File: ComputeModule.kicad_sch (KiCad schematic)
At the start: 5 parts

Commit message: assign initial footprints
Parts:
- C32: footprint (none) -> Capacitor_SMD:C_0805_2012Metric_Pad1.18x1.45mm_HandSolder
- C34: footprint (none) -> Capacitor_SMD:CP_Elec_4x5.7
- Module2: footprint (none) -> NeuralTone:CM4
- R15, R22: footprint (none) -> Resistor_SMD:R_0805_2012Metric_Pad1.20x1.40mm_HandSolder
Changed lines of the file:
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@@
       (effects (font (size 1.27 1.27)))
     )
-    (property "Footprint" "" (at 55.245 96.52 0)
+    (property "Footprint" "Resistor_SMD:R_0805_2012Metric_Pad1.20x1.40mm_HandSolder" (at 55.245 96.52 0)
       (effects (font (size 1.27 1.27)) hide)
     )
@@
       (effects (font (size 1.27 1.27)) (justify left))
     )
-    (property "Footprint" "" (at 141.605 126.365 0)
+    (property "Footprint" "Capacitor_SMD:CP_Elec_4x5.7" (at 141.605 126.365 0)
       (effects (font (size 1.27 1.27)) hide)
     )
@@
       (effects (font (size 1.27 1.27)))
     )
-    (property "Footprint" "" (at 204.47 113.03 0)
+    (property "Footprint" "NeuralTone:CM4" (at 204.47 113.03 0)
       (effects (font (size 1.27 1.27)) hide)
     )
@@
       (effects (font (size 1.27 1.27)))
     )
-    (property "Footprint" "" (at 55.245 93.98 0)
+    (property "Footprint" "Resistor_SMD:R_0805_2012Metric_Pad1.20x1.40mm_HandSolder" (at 55.245 93.98 0)
       (effects (font (size 1.27 1.27)) hide)
     )
@@
       (effects (font (size 1.27 1.27)) (justify left))
     )
-    (property "Footprint" "" (at 130.81 126.365 0)
+    (property "Footprint" "Capacitor_SMD:C_0805_2012Metric_Pad1.18x1.45mm_HandSolder" (at 130.81 126.365 0)
       (effects (font (size 1.27 1.27)) hide)
     )
@@
       (effects (font (size 1.27 1.27)))
     )
-    (property "Footprint" "" (at 100.33 113.03 0)
-      (effects (font (size 1.27 1.27)) hide)
-    )
+    (property "Footprint" "NeuralTone:CM4" (at 100.33 113.03 0)
+      (effects (font (size 1.27 1.27)) hide)
+    )

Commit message: symbol fixes
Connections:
- no-connect marks 126 -> 123
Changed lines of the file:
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@@
   (no_connect (at 168.91 114.3))
   (no_connect (at 168.91 144.78))
-  (no_connect (at 64.77 86.36))
   (no_connect (at 229.87 114.3))
   (no_connect (at 64.77 119.38))
@@
   (no_connect (at 125.73 88.9))
   (no_connect (at 64.77 45.72))
-  (no_connect (at 64.77 83.82))
   (no_connect (at 229.87 78.74))
   (no_connect (at 168.91 149.86))
@@
   (no_connect (at 64.77 48.26))
   (no_connect (at 168.91 27.94))
-  (no_connect (at 64.77 81.28))
   (no_connect (at 229.87 88.9))
   (no_connect (at 64.77 144.78))

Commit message: update elec cap footprints
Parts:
- C34: footprint Capacitor_SMD:CP_Elec_4x5.7 -> Capacitor_SMD:CP_Elec_4x5.4
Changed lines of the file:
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@@
       (effects (font (size 1.27 1.27)) (justify left))
     )
-    (property "Footprint" "Capacitor_SMD:CP_Elec_4x5.7" (at 141.605 126.365 0)
+    (property "Footprint" "Capacitor_SMD:CP_Elec_4x5.4" (at 141.605 126.365 0)
       (effects (font (size 1.27 1.27)) hide)
     )

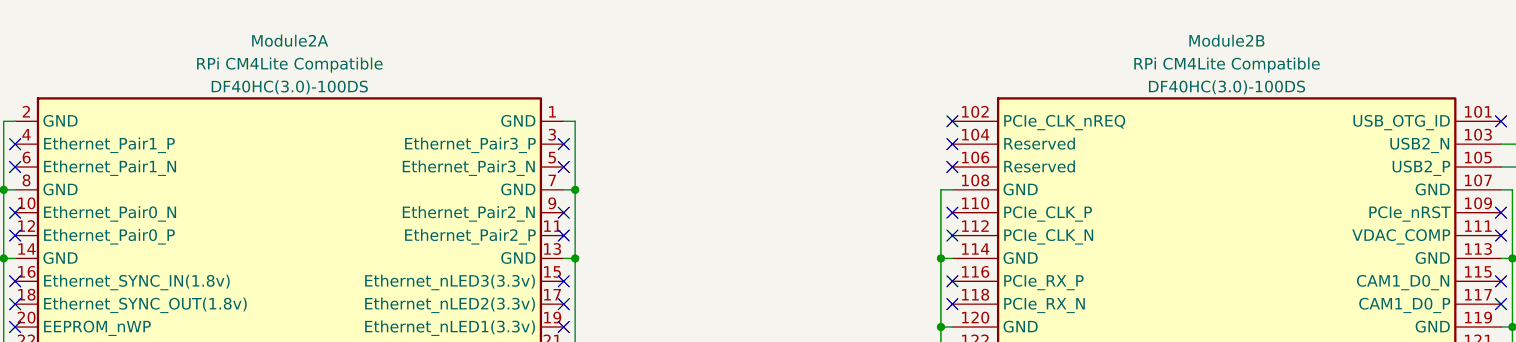
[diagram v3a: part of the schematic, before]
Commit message: redo RPi footprint
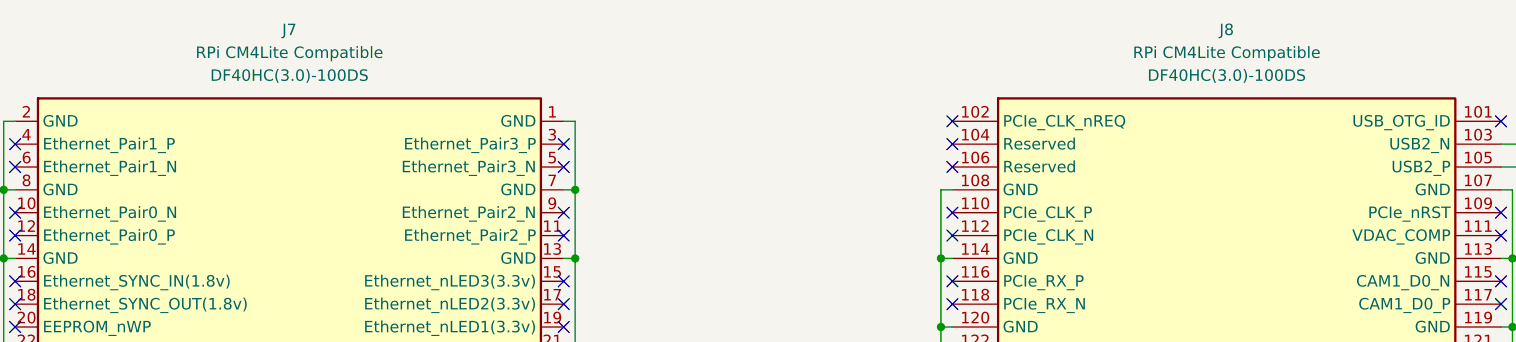
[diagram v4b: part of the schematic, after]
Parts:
- removed Module2: RPi CM4Lite Compatible, NeuralTone:CM4, symbol NeuralTone:RPi_CM4
- added J7: RPi CM4Lite Compatible, NeuralTone:DF40HC(3.0)-100DS_A, symbol NeuralTone:RPi_CM4_A
- added J8: RPi CM4Lite Compatible, NeuralTone:DF40HC(3.0)-100DS_B, symbol NeuralTone:RPi_CM4_B
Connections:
- net +3V3_CM4: now also J7.78 (GPIO_VREF(1.8v/3.3v_Input)), J7.84 (+3.3v_(Output)), J7.86 (+3.3v_(Output))
- net +5V: now also J7.77 (+5v_(Input)), J7.79 (+5v_(Input)), J7.81 (+5v_(Input)), J7.83 (+5v_(Input)), J7.85 (+5v_(Input)), J7.87 (+5v_(Input))
- net GND: now also J7.1 (GND), J7.13 (GND), J7.14 (GND), J7.2 (GND), J7.22 (GND), J7.23 (GND), J7.32 (GND), J7.33 (GND), J7.42 (GND), J7.43 (GND), J7.52 (GND), J7.53 (GND), J7.59 (GND), J7.60 (GND), J7.65 (GND), J7.66 (GND), J7.7 (GND), J7.71 (GND), J7.74 (GND), J7.8 (GND), J7.98 (GND), J8.107 (GND), J8.108 (GND), J8.113 (GND), J8.114 (GND), J8.119 (GND), J8.120 (GND), J8.125 (GND), J8.126 (GND), J8.131 (GND), J8.132 (GND), J8.137 (GND), J8.138 (GND), J8.144 (GND), J8.150 (GND), J8.155 (GND), J8.156 (GND), J8.161 (GND), J8.162 (GND), J8.167 (GND), J8.168 (GND), J8.173 (GND), J8.174 (GND), J8.179 (GND), J8.180 (GND), J8.185 (GND), J8.186 (GND), J8.191 (GND), J8.192 (GND), J8.197 (GND), J8.198 (GND)
- net I2S_BCK: now also J7.49 (GPIO18)
- net I2S_DIN: now also J7.27 (GPIO20)
- net I2S_DOUT: now also J7.25 (GPIO21)
- net I2S_LRCK: now also J7.26 (GPIO19)
- net LED_STAT_1: now also J7.46 (GPIO22)
- net LED_STAT_2: now also J7.48 (GPIO27)
- net MULTI_BTN: now also J7.50 (GPIO17)
- net SD_CLK: now also J7.57 (SD_CLK)
- net SD_CMD: now also J7.62 (SD_CMD)
- net SD_DAT0: now also J7.63 (SD_DAT0)
- net SD_DAT1: now also J7.67 (SD_DAT1)
- net SD_DAT2: now also J7.69 (SD_DAT2)
- net SD_DAT3: now also J7.61 (SD_DAT3)
- net USBD+: now also J8.105 (USB2_P)
- net USBD-: now also J8.103 (USB2_N)
- net at R15.2: now also J7.58 (GPIO2)
- net at R22.2: now also J7.56 (GPIO3)

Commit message: better decoupling strategy
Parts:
- removed C34: 4.7u, Capacitor_SMD:CP_Elec_4x5.4, symbol Device:C_Polarized_Small
- C32: value 100n -> 470n

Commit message: overall value adjustments
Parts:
- C32: value 470n -> 4.7u

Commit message: update to a proper USB PD chip
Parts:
- removed C32: 4.7u, Capacitor_SMD:C_0805_2012Metric_Pad1.18x1.45mm_HandSolder, symbol Device:C_Small
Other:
- note added: "NOTE: Module has built-in decoupling"
